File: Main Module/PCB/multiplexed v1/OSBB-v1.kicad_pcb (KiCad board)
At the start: 2 copper layers, 85.6 x 49.8 mm, 170 parts, among them P1 AUX 1-3, P14 EXTRA Pins, P2 Wire to Teensy VUSB, P3 +3.3V, P4 Pit, P5 Encoders, P6 BTN 1-32, Q1 NPN, Q2 NPN, Q3 NPN, Q4 NPN, U1 74HC4051, U2 74HC4051, U3 74HC4051, U4 74HC4051, U5 Teensy3.2

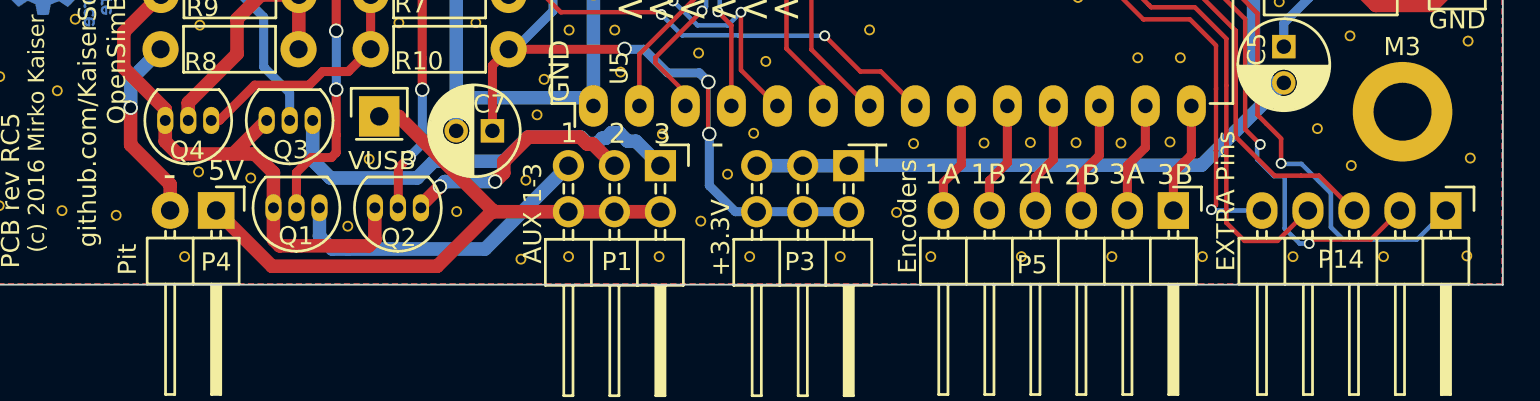
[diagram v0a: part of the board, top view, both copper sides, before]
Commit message: * added a few labels since I don't export all vlues for the gerber files * gerber files for RC5
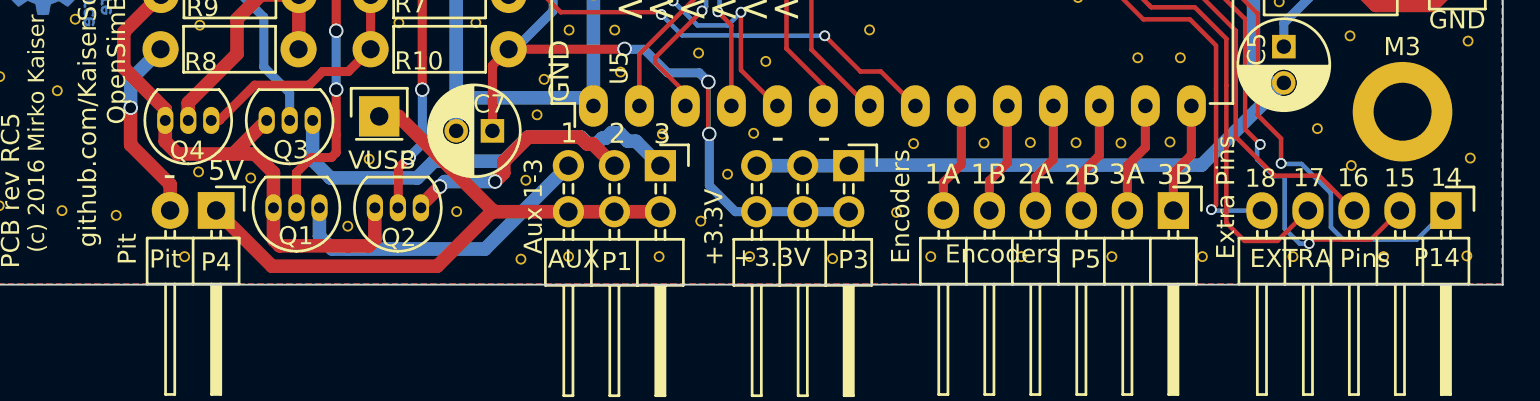
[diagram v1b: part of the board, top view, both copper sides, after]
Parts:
- P1: value AUX 1-3 -> AUX
- moved Ref** 0.43 mm to (223.9, 143.3)
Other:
- board text added: "+3.3V"
- board text added: "Aux 1-3"
- board text added: "Encoders"
- board text added: "Extra Pins"
- board text added: "Pit"
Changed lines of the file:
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@@
     (area 175.269999 88.074999 261.407144 151.803575)
     (thickness 1.6)
-    (drawings 96)
+    (drawings 106)
     (tracks 1158)
     (zones 0)
@@
       (drillshape 0)
       (scaleselection 1)
-      (outputdirectory ../Gerber-rev-RC4/))
+      (outputdirectory gerber/RC5/))
   )
   (net 0 "")
@@
   )
   (module MOBB-KiCad-Lib:VIA-W0.6mm-H0.4mm (layer F.Cu)
-    (at 224.33 143.22)
+    (at 223.91 143.33)
     (fp_text reference Ref** (at 0 0.5) (layer F.Fab) hide
       (effects (font (size 0.127 0.127) (thickness 0.000001)))
@@
       (effects (font (size 1 1) (thickness 0.15)))
     )
-    (fp_text value Pit (at 2.705 4.895 270) (layer F.SilkS)
+    (fp_text value Pit (at 2.69 2.82 360) (layer F.SilkS)
       (effects (font (size 1 1) (thickness 0.15)))
     )
@@
     (descr "Through hole pin header")
     (tags "pin header")
-    (fp_text reference P5 (at 3 7.8 360) (layer F.SilkS)
+    (fp_text reference P5 (at 2.685 4.845 360) (layer F.SilkS)
       (effects (font (size 1 1) (thickness 0.15)))
     )
-    (fp_text value Encoders (at 0.325 14.675 270) (layer F.SilkS)
+    (fp_text value Encoders (at 2.405 9.455 360) (layer F.SilkS)
       (effects (font (size 1 1) (thickness 0.15)))
     )
@@
       (effects (font (size 1 1) (thickness 0.15)))
     )
-    (fp_text value "AUX 1-3" (at 2.625 7.05 270) (layer F.SilkS)
+    (fp_text value AUX (at 5.16 4.78 360) (layer F.SilkS)
       (effects (font (size 1 1) (thickness 0.15)))
     )
@@
     (descr "Through hole pin header")
     (tags "pin header")
-    (fp_text reference P3 (at 5.3 2.7 360) (layer F.SilkS)
+    (fp_text reference P3 (at 5.19 -0.26 360) (layer F.SilkS)
       (effects (font (size 1 1) (thickness 0.15)))
     )
-    (fp_text value +3.3V (at 3.975 7.075 270) (layer F.SilkS)
+    (fp_text value +3.3V (at 5.07 4.23 360) (layer F.SilkS)
       (effects (font (size 1 1) (thickness 0.15)))
     )
@@
     (descr "Through hole pin header")
     (tags "pin header")
-    (fp_text reference P14 (at 2.7 5.8 360) (layer F.SilkS)
+    (fp_text reference P14 (at 2.605 0.505 360) (layer F.SilkS)
       (effects (font (size 1 1) (thickness 0.15)))
     )
-    (fp_text value "EXTRA Pins" (at -0.525 12.15 270) (layer F.SilkS)
+    (fp_text value "EXTRA Pins" (at 2.655 6.955 360) (layer F.SilkS)
       (effects (font (size 1 1) (thickness 0.15)))
     )
@@
       (net 6 GND) (zone_connect 2))
   )
+  (gr_text 14 (at 257.8 138.85) (layer F.SilkS)
+    (effects (font (size 1 1) (thickness 0.25)))
+  )
+  (gr_text 15 (at 255.22 138.88) (layer F.SilkS)
+    (effects (font (size 1 1) (thickness 0.25)))
+  )
+  (gr_text 16 (at 252.65 138.87) (layer F.SilkS)
+    (effects (font (size 1 1) (thickness 0.25)))
+  )
+  (gr_text 17 (at 250.21 138.87) (layer F.SilkS)
+    (effects (font (size 1 1) (thickness 0.25)))
+  )
+  (gr_text 18 (at 247.54 138.9) (layer F.SilkS)
+    (effects (font (size 1 1) (thickness 0.25)))
+  )
+  (gr_text "Extra Pins" (at 245.62 139.95 90) (layer F.SilkS)
+    (effects (font (size 1 1) (thickness 0.25)))
+  )
+  (gr_text Encoders (at 227.67 140.45 90) (layer F.SilkS)
+    (effects (font (size 1 1) (thickness 0.25)))
+  )
+  (gr_text +3.3V (at 217.36 141.6 90) (layer F.SilkS)
+    (effects (font (size 1 1) (thickness 0.25)))
+  )
+  (gr_text "Aux 1-3" (at 207.39 140.44 90) (layer F.SilkS)
+    (effects (font (size 1 1) (thickness 0.25)))
+  )
+  (gr_text Pit (at 184.97 142.8 90) (layer F.SilkS)
+    (effects (font (size 1 1) (thickness 0.25)))
+  )
   (gr_line (start 227.28 132.24) (end 227.28 129.5) (angle 90) (layer F.Fab) (width 0.2))
   (gr_line (start 239.14 132.24) (end 227.28 132.24) (angle 90) (layer F.Fab) (width 0.2))
@@
     (effects (font (size 1.2 1.2) (thickness 0.25)) (justify mirror))
   )
-  (gr_text - (at 226.65 136.925) (layer F.SilkS)
+  (gr_text - (at 223.44 136.61) (layer F.SilkS)
     (effects (font (size 1.5 1.5) (thickness 0.3)))
   )
-  (gr_text - (at 217.55 136.925) (layer F.SilkS)
+  (gr_text - (at 220.88 136.61) (layer F.SilkS)
     (effects (font (size 1.5 1.5) (thickness 0.3)))
   )
@@
     (effects (font (size 1 1) (thickness 0.25)))
   )
-  (gr_text VUSB (at 199.025 137.925) (layer F.SilkS)
+  (gr_text VUSB (at 199.03 137.9) (layer F.SilkS)
     (effects (font (size 1 1) (thickness 0.2)))
   )

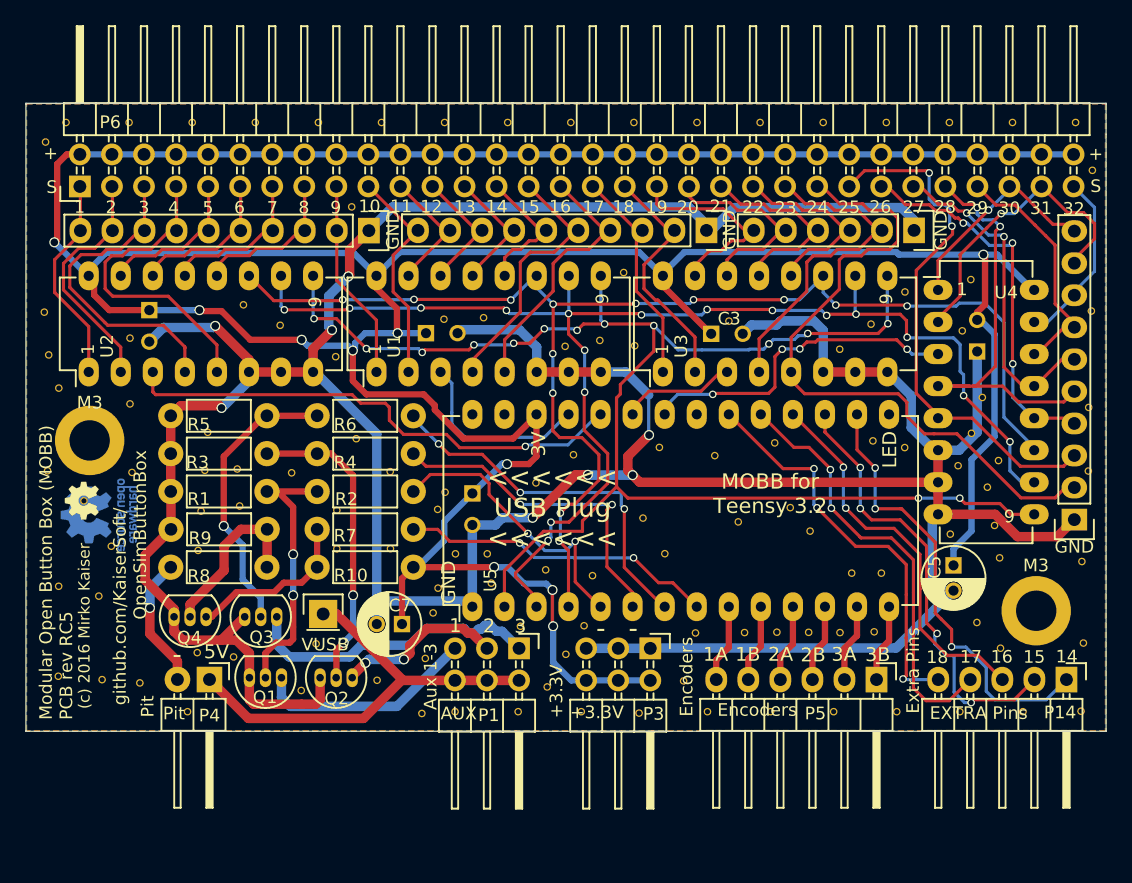
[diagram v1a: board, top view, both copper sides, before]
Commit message: * current work of PCB RC6 - WIP * added PTC fuses for 3.3V and 5V to protect the PC in case of accidental short circuit * added 2x1 straight pin header which connects to pin13. this may late be used for feedback. not used yet * added solder pads for optional SMD 0805 capacitors * position of mounting holes has moved again. now final and written on PCB back side * distance between pit, AUX, encoder, .... pin headers now multiples of 2.54mm
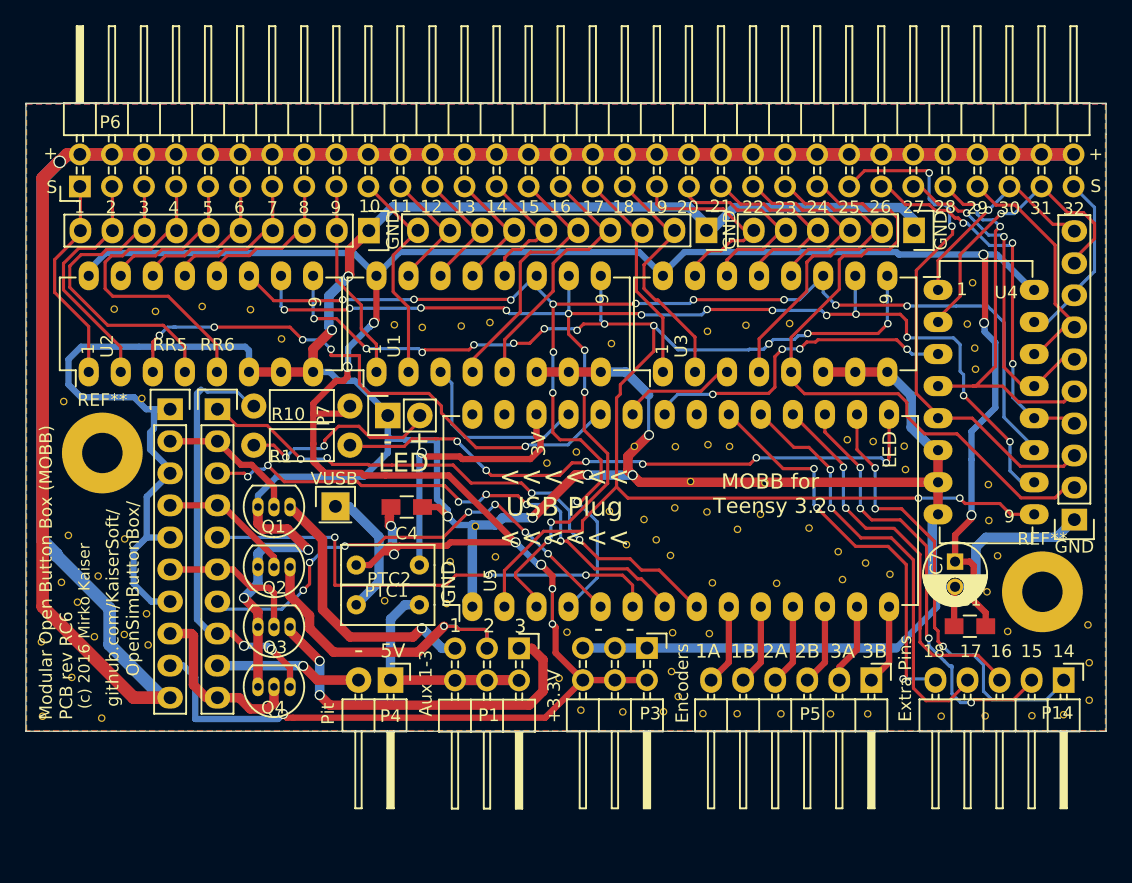
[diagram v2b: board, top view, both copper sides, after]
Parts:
- removed C2, C3, C6: C, Capacitors_ThroughHole:C_Disc_D3_P2.5
- removed C5: CP, Capacitors_ThroughHole:C_Radial_D5_L11_P2
- removed G***: LOGO, MOBB-KiCad-Lib:OPEN_HW_LOGO_3MM
- removed R2, R4, R6, R7, R8: 1K, Resistors_ThroughHole:Resistor_Horizontal_RM7mm
- removed R3, R5, R9: 10K, Resistors_ThroughHole:Resistor_Horizontal_RM7mm
- removed the REF** at (180.4, 121.7)
- removed the REF** at (255.4, 135.2)
- removed REF***: OSHW-Logo_5.7x6mm_Copper, Symbols:OSHW-Logo_5.7x6mm_Copper
- removed the Ref** at (252.4, 123.3)
- removed the Ref** at (229.3, 143.2)
- removed the Ref** at (177.9, 133.3)
- removed the Ref** at (177.9, 140.4)
- removed the Ref** at (184.3, 140.9)
- removed the Ref** at (188.1, 143.2)
- removed the Ref** at (188.9, 138.5)
- removed the Ref** at (191.8, 138.9)
- removed the Ref** at (198.3, 137.8)
- removed the Ref** at (197.1, 141.5)
- removed the Ref** at (206.7, 143.4)
- removed the Ref** at (209.3, 143.2)
- removed the Ref** at (223.9, 143.3)
- removed the Ref** at (214.5, 136.4)
- removed the Ref** at (219.6, 136.4)
- removed the Ref** at (218.1, 138.7)
- removed the Ref** at (216.6, 141.3)
- removed the Ref** at (228.4, 137.0)
- removed the Ref** at (227.4, 140.8)
- removed the Ref** at (252.6, 138.2)
- removed the Ref** at (250.7, 136.2)
- removed the Ref** at (259.1, 137.8)
- removed the Ref** at (259.0, 131.3)
- removed the Ref** at (219.3, 143.2)
- removed the Ref** at (252.5, 131.0)
- removed the Ref** at (252.1, 128.5)
- removed the Ref** at (248.6, 129.2)
- removed the Ref** at (235.9, 127.0)
- removed the Ref** at (237.5, 128.9)
- removed the Ref** at (231.8, 128.2)
- removed the Ref** at (225.9, 130.7)
- removed the Ref** at (243.1, 132.2)
- removed the Ref** at (240.8, 132.2)
- removed the Ref** at (224.2, 127.9)
- removed the Ref** at (214.3, 143.2)
- removed the Ref** at (178.5, 96.5)
- removed the Ref** at (183.5, 96.5)
- removed the Ref** at (188.5, 96.5)
- removed the Ref** at (193.5, 96.5)
- removed the Ref** at (198.5, 96.5)
- removed the Ref** at (203.5, 96.5)
- removed the Ref** at (250.2, 121.2)
- removed the Ref** at (208.5, 96.5)
- removed the Ref** at (213.5, 96.5)
- removed the Ref** at (218.5, 96.5)
- removed the Ref** at (223.5, 96.5)
- removed the Ref** at (228.5, 96.5)
- removed the Ref** at (233.5, 96.5)
- removed the Ref** at (238.5, 96.5)
- removed the Ref** at (243.5, 96.5)
- removed the Ref** at (248.5, 96.5)
- removed the Ref** at (253.5, 96.5)
- removed the Ref** at (251.1, 118.3)
- removed the Ref** at (245.0, 110.0)
- removed the Ref** at (222.7, 108.4)
- removed the Ref** at (200.0, 130.3)
- removed the Ref** at (200.0, 127.3)
- removed the Ref** at (196.4, 124.3)
- removed the Ref** at (192.1, 124.0)
- removed the Ref** at (192.3, 126.9)
- removed the Ref** at (207.0, 139.0)
- removed the Ref** at (203.2, 140.7)
- removed the Ref** at (242.5, 136.9)
- removed the Ref** at (258.9, 143.2)
- removed the Ref** at (239.8, 136.9)
- removed the Ref** at (237.3, 136.9)
- removed the Ref** at (234.8, 136.9)
- removed the Ref** at (232.3, 136.9)
- removed the Ref** at (245.0, 122.3)
- removed the Ref** at (242.4, 121.8)
- removed the Ref** at (201.1, 103.2)
- removed the Ref** at (234.7, 121.9)
- removed the Ref** at (249.2, 123.7)
- removed the Ref** at (251.5, 125.4)
- removed the Ref** at (254.3, 143.2)
- removed the Ref** at (259.5, 124.2)
- removed the Ref** at (259.5, 119.1)
- removed the Ref** at (259.8, 111.5)
- removed the Ref** at (250.2, 109.0)
- removed the Ref** at (249.5, 113.0)
- removed the Ref** at (242.3, 112.5)
- removed the Ref** at (239.8, 114.5)
- removed the Ref** at (231.0, 112.3)
- removed the Ref** at (223.6, 114.2)
- removed the Ref** at (220.8, 113.8)
- removed the Ref** at (249.3, 143.2)
- removed the Ref** at (218.1, 114.3)
- removed the Ref** at (208.4, 112.1)
- removed the Ref** at (211.6, 112.0)
- removed the Ref** at (199.9, 115.1)
- removed the Ref** at (195.5, 112.6)
- removed the Ref** at (192.6, 111.0)
- removed the Ref** at (183.6, 113.6)
- removed the Ref** at (183.7, 124.3)
- removed the Ref** at (183.6, 118.8)
- removed the Ref** at (177.9, 117.6)
- removed the Ref** at (244.3, 143.2)
- removed the Ref** at (189.7, 121.1)
- removed the Ref** at (189.5, 124.1)
- removed the Ref** at (189.2, 127.3)
- removed the Ref** at (189.0, 130.4)
- removed the Ref** at (204.2, 130.3)
- removed the Ref** at (204.2, 124.2)
- removed the Ref** at (201.5, 121.6)
- removed the Ref** at (220.2, 132.4)
- removed the Ref** at (216.5, 132.0)
- removed the Ref** at (209.4, 130.7)
- removed the Ref** at (239.3, 143.2)
- removed the Ref** at (211.9, 130.7)
- removed the Ref** at (212.2, 133.0)
- removed the Ref** at (207.6, 135.4)
- removed the Ref** at (208.0, 133.4)
- removed the Ref** at (207.9, 127.2)
- removed the Ref** at (208.5, 125.8)
- removed the Ref** at (215.7, 125.1)
- removed the Ref** at (218.7, 122.9)
- removed the Ref** at (229.9, 122.9)
- removed the Ref** at (225.5, 122.3)
- removed the Ref** at (234.3, 143.2)
- removed the Ref** at (259.8, 100.3)
- removed the Ref** at (258.5, 96.5)
- removed the Ref** at (176.9, 98.1)
- removed the Ref** at (176.8, 111.6)
- removed the Ref** at (177.1, 115.0)
- removed the Ref** at (177.0, 124.1)
- removed the Ref** at (179.9, 126.5)
- removed the Ref** at (182.1, 130.1)
- removed the Ref** at (181.4, 140.7)
- removed the Ref** at (181.1, 134.1)
- added P7: LED, Pin_Headers:Pin_Header_Straight_1x02, F.Cu at (204.0, 119.8)
- added PTC1: h0.3A/t0.5A, MOBB-KiCad-Lib:PTC-5MM, F.Cu at (204.0, 134.8)
- added PTC2: h0.3A/t0.5A, MOBB-KiCad-Lib:PTC-5MM, F.Cu at (204.0, 131.6)
- added REF**: MountingHole_3.2mm_M3_Pad, Mounting_Holes:MountingHole_3.2mm_M3_Pad, F.Cu at (181.4, 122.7)
- added REF**: MountingHole_3.2mm_M3_Pad, Mounting_Holes:MountingHole_3.2mm_M3_Pad, F.Cu at (255.9, 133.7)
- added RR5: 10K-STAR10, Pin_Headers:Pin_Header_Straight_1x10, F.Cu at (186.8, 119.2)
- added RR6: 1K-STAR10, Pin_Headers:Pin_Header_Straight_1x10, F.Cu at (190.5, 119.2)
- added Ref**: Val**, MOBB-KiCad-Lib:VIA-W0.6mm-H0.4mm, F.Cu at (251.5, 133.7)
- added Ref**: Val**, MOBB-KiCad-Lib:VIA-W0.6mm-H0.4mm, F.Cu at (229.4, 122.1)
- added Ref**: Val**, MOBB-KiCad-Lib:VIA-W0.6mm-H0.4mm, F.Cu at (223.5, 122.2)
- added Ref**: Val**, MOBB-KiCad-Lib:VIA-W0.6mm-H0.4mm, F.Cu at (225.3, 129.6)
- added Ref**: Val**, MOBB-KiCad-Lib:VIA-W0.6mm-H0.4mm, F.Cu at (229.3, 127.4)
- added Ref**: Val**, MOBB-KiCad-Lib:VIA-W0.6mm-H0.4mm, F.Cu at (233.5, 127.6)
- added Ref**: Val**, MOBB-KiCad-Lib:VIA-W0.6mm-H0.4mm, F.Cu at (195.6, 113.7)
- added Ref**: Val**, MOBB-KiCad-Lib:VIA-W0.6mm-H0.4mm, F.Cu at (183.2, 129.5)
- added Ref**: Val**, MOBB-KiCad-Lib:VIA-W0.6mm-H0.4mm, F.Cu at (208.9, 131.3)
- added Ref**: Val**, MOBB-KiCad-Lib:VIA-W0.6mm-H0.4mm, F.Cu at (216.6, 123.5)
- added Ref**: Val**, MOBB-KiCad-Lib:VIA-W0.6mm-H0.4mm, F.Cu at (218.9, 122.6)
- added Ref**: Val**, MOBB-KiCad-Lib:VIA-W0.6mm-H0.4mm, F.Cu at (253.1, 136.9)
- added Ref**: Val**, MOBB-KiCad-Lib:VIA-W0.6mm-H0.4mm, F.Cu at (210.9, 128.5)
- added Ref**: Val**, MOBB-KiCad-Lib:VIA-W0.6mm-H0.4mm, F.Cu at (203.8, 134.4)
- added Ref**: Val**, MOBB-KiCad-Lib:VIA-W0.6mm-H0.4mm, F.Cu at (208.7, 134.7)
- added Ref**: Val**, MOBB-KiCad-Lib:VIA-W0.6mm-H0.4mm, F.Cu at (226.5, 140.0)
- added Ref**: Val**, MOBB-KiCad-Lib:VIA-W0.6mm-H0.4mm, F.Cu at (227.0, 142.0)
- added Ref**: Val**, MOBB-KiCad-Lib:VIA-W0.6mm-H0.4mm, F.Cu at (224.3, 128.0)
- added Ref**: Val**, MOBB-KiCad-Lib:VIA-W0.6mm-H0.4mm, F.Cu at (226.7, 127.1)
- added Ref**: Val**, MOBB-KiCad-Lib:VIA-W0.6mm-H0.4mm, F.Cu at (217.6, 140.6)
- added Ref**: Val**, MOBB-KiCad-Lib:VIA-W0.6mm-H0.4mm, F.Cu at (218.2, 136.9)
- added Ref**: Val**, MOBB-KiCad-Lib:VIA-W0.6mm-H0.4mm, F.Cu at (229.7, 133.0)
- added Ref**: Val**, MOBB-KiCad-Lib:VIA-W0.6mm-H0.4mm, F.Cu at (184.5, 118.4)
- added Ref**: Val**, MOBB-KiCad-Lib:VIA-W0.6mm-H0.4mm, F.Cu at (234.8, 133.1)
- added Ref**: Val**, MOBB-KiCad-Lib:VIA-W0.6mm-H0.4mm, F.Cu at (240.0, 132.8)
- added Ref**: Val**, MOBB-KiCad-Lib:VIA-W0.6mm-H0.4mm, F.Cu at (226.6, 137.0)
- added Ref**: Val**, MOBB-KiCad-Lib:VIA-W0.6mm-H0.4mm, F.Cu at (229.5, 137.0)
- added Ref**: Val**, MOBB-KiCad-Lib:VIA-W0.6mm-H0.4mm, F.Cu at (219.3, 143.1)
- added Ref**: Val**, MOBB-KiCad-Lib:VIA-W0.6mm-H0.4mm, F.Cu at (222.6, 143.2)
- added Ref**: Val**, MOBB-KiCad-Lib:VIA-W0.6mm-H0.4mm, F.Cu at (225.8, 143.2)
- added Ref**: Val**, MOBB-KiCad-Lib:VIA-W0.6mm-H0.4mm, F.Cu at (229.0, 143.4)
- added Ref**: Val**, MOBB-KiCad-Lib:VIA-W0.6mm-H0.4mm, F.Cu at (231.7, 143.4)
- added Ref**: Val**, MOBB-KiCad-Lib:VIA-W0.6mm-H0.4mm, F.Cu at (235.2, 143.4)
- added Ref**: Val**, MOBB-KiCad-Lib:VIA-W0.6mm-H0.4mm, F.Cu at (184.9, 135.5)
- added Ref**: Val**, MOBB-KiCad-Lib:VIA-W0.6mm-H0.4mm, F.Cu at (239.1, 143.4)
- added Ref**: Val**, MOBB-KiCad-Lib:VIA-W0.6mm-H0.4mm, F.Cu at (242.0, 143.4)
- added Ref**: Val**, MOBB-KiCad-Lib:VIA-W0.6mm-H0.4mm, F.Cu at (247.8, 143.6)
- added Ref**: Val**, MOBB-KiCad-Lib:VIA-W0.6mm-H0.4mm, F.Cu at (251.3, 143.6)
- added Ref**: Val**, MOBB-KiCad-Lib:VIA-W0.6mm-H0.4mm, F.Cu at (255.0, 143.5)
- added Ref**: Val**, MOBB-KiCad-Lib:VIA-W0.6mm-H0.4mm, F.Cu at (257.6, 143.5)
- added Ref**: Val**, MOBB-KiCad-Lib:VIA-W0.6mm-H0.4mm, F.Cu at (259.6, 142.3)
- added Ref**: Val**, MOBB-KiCad-Lib:VIA-W0.6mm-H0.4mm, F.Cu at (259.5, 136.3)
- added Ref**: Val**, MOBB-KiCad-Lib:VIA-W0.6mm-H0.4mm, F.Cu at (259.6, 139.3)
- added Ref**: Val**, MOBB-KiCad-Lib:VIA-W0.6mm-H0.4mm, F.Cu at (245.0, 124.0)
- added Ref**: Val**, MOBB-KiCad-Lib:VIA-W0.6mm-H0.4mm, F.Cu at (185.0, 137.9)
- added Ref**: Val**, MOBB-KiCad-Lib:VIA-W0.6mm-H0.4mm, F.Cu at (244.9, 122.2)
- added Ref**: Val**, MOBB-KiCad-Lib:VIA-W0.6mm-H0.4mm, F.Cu at (242.5, 121.8)
- added Ref**: Val**, MOBB-KiCad-Lib:VIA-W0.6mm-H0.4mm, F.Cu at (240.4, 121.7)
- added Ref**: Val**, MOBB-KiCad-Lib:VIA-W0.6mm-H0.4mm, F.Cu at (231.1, 122.2)
- added Ref**: Val**, MOBB-KiCad-Lib:VIA-W0.6mm-H0.4mm, F.Cu at (226.8, 122.2)
- added Ref**: Val**, MOBB-KiCad-Lib:VIA-W0.6mm-H0.4mm, F.Cu at (233.9, 125.1)
- added Ref**: Val**, MOBB-KiCad-Lib:VIA-W0.6mm-H0.4mm, F.Cu at (228.0, 125.0)
- added Ref**: Val**, MOBB-KiCad-Lib:VIA-W0.6mm-H0.4mm, F.Cu at (212.5, 130.9)
- added Ref**: Val**, MOBB-KiCad-Lib:VIA-W0.6mm-H0.4mm, F.Cu at (221.6, 127.3)
- added Ref**: Val**, MOBB-KiCad-Lib:VIA-W0.6mm-H0.4mm, F.Cu at (222.9, 130.0)
- added Ref**: Val**, MOBB-KiCad-Lib:VIA-W0.6mm-H0.4mm, F.Cu at (183.1, 137.1)
- added Ref**: Val**, MOBB-KiCad-Lib:VIA-W0.6mm-H0.4mm, F.Cu at (226.4, 130.8)
- added Ref**: Val**, MOBB-KiCad-Lib:VIA-W0.6mm-H0.4mm, F.Cu at (231.7, 128.8)
- added Ref**: Val**, MOBB-KiCad-Lib:VIA-W0.6mm-H0.4mm, F.Cu at (237.4, 128.7)
- added Ref**: Val**, MOBB-KiCad-Lib:VIA-W0.6mm-H0.4mm, F.Cu at (239.7, 130.5)
- added Ref**: Val**, MOBB-KiCad-Lib:VIA-W0.6mm-H0.4mm, F.Cu at (241.9, 131.4)
- added Ref**: Val**, MOBB-KiCad-Lib:VIA-W0.6mm-H0.4mm, F.Cu at (243.8, 132.3)
- added Ref**: Val**, MOBB-KiCad-Lib:VIA-W0.6mm-H0.4mm, F.Cu at (252.3, 130.9)
- added Ref**: Val**, MOBB-KiCad-Lib:VIA-W0.6mm-H0.4mm, F.Cu at (251.6, 128.1)
- added Ref**: Val**, MOBB-KiCad-Lib:VIA-W0.6mm-H0.4mm, F.Cu at (251.6, 125.2)
- added Ref**: Val**, MOBB-KiCad-Lib:VIA-W0.6mm-H0.4mm, F.Cu at (250.3, 109.2)
- added Ref**: Val**, MOBB-KiCad-Lib:VIA-W0.6mm-H0.4mm, F.Cu at (181.1, 132.5)
- added Ref**: Val**, MOBB-KiCad-Lib:VIA-W0.6mm-H0.4mm, F.Cu at (250.6, 116.1)
- added Ref**: Val**, MOBB-KiCad-Lib:VIA-W0.6mm-H0.4mm, F.Cu at (250.5, 114.4)
- added Ref**: Val**, MOBB-KiCad-Lib:VIA-W0.6mm-H0.4mm, F.Cu at (249.9, 112.5)
- added Ref**: Val**, MOBB-KiCad-Lib:VIA-W0.6mm-H0.4mm, F.Cu at (235.8, 112.5)
- added Ref**: Val**, MOBB-KiCad-Lib:VIA-W0.6mm-H0.4mm, F.Cu at (232.4, 112.6)
- added Ref**: Val**, MOBB-KiCad-Lib:VIA-W0.6mm-H0.4mm, F.Cu at (229.3, 113.1)
- added Ref**: Val**, MOBB-KiCad-Lib:VIA-W0.6mm-H0.4mm, F.Cu at (221.7, 114.0)
- added Ref**: Val**, MOBB-KiCad-Lib:VIA-W0.6mm-H0.4mm, F.Cu at (212.1, 112.4)
- added Ref**: Val**, MOBB-KiCad-Lib:VIA-W0.6mm-H0.4mm, F.Cu at (209.8, 112.7)
- added Ref**: Val**, MOBB-KiCad-Lib:VIA-W0.6mm-H0.4mm, F.Cu at (206.7, 112.8)
- added Ref**: Val**, MOBB-KiCad-Lib:VIA-W0.6mm-H0.4mm, F.Cu at (179.4, 134.5)
- added Ref**: Val**, MOBB-KiCad-Lib:VIA-W0.6mm-H0.4mm, F.Cu at (204.5, 112.6)
- added Ref**: Val**, MOBB-KiCad-Lib:VIA-W0.6mm-H0.4mm, F.Cu at (193.1, 111.4)
- added Ref**: Val**, MOBB-KiCad-Lib:VIA-W0.6mm-H0.4mm, F.Cu at (189.3, 111.1)
- added Ref**: Val**, MOBB-KiCad-Lib:VIA-W0.6mm-H0.4mm, F.Cu at (185.6, 111.5)
- added Ref**: Val**, MOBB-KiCad-Lib:VIA-W0.6mm-H0.4mm, F.Cu at (182.3, 111.3)
- added Ref**: Val**, MOBB-KiCad-Lib:VIA-W0.6mm-H0.4mm, F.Cu at (178.3, 118.6)
- added Ref**: Val**, MOBB-KiCad-Lib:VIA-W0.6mm-H0.4mm, F.Cu at (178.7, 129.2)
- added Ref**: Val**, MOBB-KiCad-Lib:VIA-W0.6mm-H0.4mm, F.Cu at (181.3, 143.7)
- added Ref**: Val**, MOBB-KiCad-Lib:VIA-W0.6mm-H0.4mm, F.Cu at (179.0, 140.5)
- added Ref**: Val**, MOBB-KiCad-Lib:VIA-W0.6mm-H0.4mm, F.Cu at (176.6, 137.7)
- added Ref**: Val**, MOBB-KiCad-Lib:VIA-W0.6mm-H0.4mm, F.Cu at (176.6, 143.6)
- added Ref**: Val**, MOBB-KiCad-Lib:VIA-W0.6mm-H0.4mm, F.Cu at (180.8, 137.3)
- added Ref**: Val**, MOBB-KiCad-Lib:VIA-W0.6mm-H0.4mm, F.Cu at (178.1, 133.0)
- C1, C4: footprint Capacitors_ThroughHole:C_Disc_D3_P2.5 -> Capacitors_SMD:C_0805_HandSoldering; moved to F.Cu
- P1: value AUX -> AUX 1-3
- P4: value Pit -> Pit Limiter
- P5: value Encoders -> Rotary Encoders
- moved C1 69.7 mm to (250.1, 136.4), turned to 0 degrees
- moved C4 46.9 mm to (205.5, 127.0), turned to 180 degrees
- moved C7 44.1 mm to (248.9, 131.3), turned to 270 degrees
- moved P4 14.3 mm to (204.2, 140.7)
- moved R10 13.7 mm to (201.0, 119.0)
- moved Q1 13.5 mm to (196.2, 127.0)
- moved Q2 10.1 mm to (196.2, 131.8)
- moved Q4 8.66 mm to (196.2, 141.2)
- moved P2 8.58 mm to (199.8, 127.0)
- moved R1 7.53 mm to (201.0, 122.1)
- moved Q3 1.32 mm to (196.2, 136.5)
- moved P5 0.41 mm to (242.3, 140.7)
- moved P3 0.27 mm to (224.5, 138.2)
- moved P14 0.22 mm to (257.6, 140.7)
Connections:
- C1 pad 1: +3V3 -> GND
- C1 pad 2: GND -> +3V3
- P2 pad 1: +5V -> Net-(P2-Pad1)
- P6 pad 10: +3V3 -> PINHEADERSRC
- P6 pad 12: +3V3 -> PINHEADERSRC
- P6 pad 14: +3V3 -> PINHEADERSRC
- P6 pad 16: +3V3 -> PINHEADERSRC
- P6 pad 18: +3V3 -> PINHEADERSRC
- P6 pad 2: +3V3 -> PINHEADERSRC
- P6 pad 20: +3V3 -> PINHEADERSRC
- P6 pad 22: +3V3 -> PINHEADERSRC
- P6 pad 24: +3V3 -> PINHEADERSRC
- P6 pad 26: +3V3 -> PINHEADERSRC
- P6 pad 28: +3V3 -> PINHEADERSRC
- P6 pad 30: +3V3 -> PINHEADERSRC
- P6 pad 32: +3V3 -> PINHEADERSRC
- P6 pad 34: +3V3 -> PINHEADERSRC
- P6 pad 36: +3V3 -> PINHEADERSRC
- P6 pad 38: +3V3 -> PINHEADERSRC
- P6 pad 4: +3V3 -> PINHEADERSRC
- P6 pad 40: +3V3 -> PINHEADERSRC
- P6 pad 42: +3V3 -> PINHEADERSRC
- P6 pad 44: +3V3 -> PINHEADERSRC
- P6 pad 46: +3V3 -> PINHEADERSRC
- P6 pad 48: +3V3 -> PINHEADERSRC
- P6 pad 50: +3V3 -> PINHEADERSRC
- P6 pad 52: +3V3 -> PINHEADERSRC
- P6 pad 54: +3V3 -> PINHEADERSRC
- P6 pad 56: +3V3 -> PINHEADERSRC
- P6 pad 58: +3V3 -> PINHEADERSRC
- P6 pad 6: +3V3 -> PINHEADERSRC
- P6 pad 60: +3V3 -> PINHEADERSRC
- P6 pad 62: +3V3 -> PINHEADERSRC
- P6 pad 64: +3V3 -> PINHEADERSRC
- P6 pad 8: +3V3 -> PINHEADERSRC
- R1 pad 1: Net-(Q1-Pad2) -> Net-(R1-Pad1)
- R1 pad 2: GND -> Net-(P7-Pad2)
- U5 pad 15: Net-(U5-Pad15) -> Net-(R1-Pad1)
- U5 pad 21: /reserved_for_4051 -> (no net)
- U5 pad 26: +3V3 -> Net-(PTC2-Pad2)
- U5 pad 27: Net-(U5-Pad27) -> (no net)
- U5 pad 28: Net-(U5-Pad28) -> (no net)
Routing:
- net PINHEADERSRC: track 0.00 -> 334.6 mm, vias 0 -> 1
- net +3V3: track 311.8 -> 236.6 mm, vias 10 -> 12
- net Net-(R1-Pad1): track 0.00 -> 49.1 mm, vias 0 -> 6
- net Net-(PTC2-Pad2): track 0.00 -> 22.4 mm, vias 0 -> 1
- net Net-(RR6-Pad1): track 25.3 -> 45.8 mm, vias 2 -> 4
- net Net-(Q4-Pad1): track 13.4 -> 33.3 mm, vias 0 -> 2
- net Net-(P7-Pad2): track 0.00 -> 16.2 mm, vias 0 -> 2
- net Net-(RR6-Pad7): track 22.7 -> 38.5 mm, vias 2 -> 7
- net Net-(P1-Pad3): track 13.6 -> 27.6 mm, vias 2 -> 1
- net Net-(Q2-Pad2): track 24.1 -> 10.3 mm, vias 2 -> 0
- net Net-(RR6-Pad3): track 29.7 -> 43.3 mm, vias 3 -> 6
- net +5V: track 35.9 -> 22.9 mm
- net Net-(RR6-Pad5): track 26.6 -> 39.1 mm, vias 2 -> 3
- net Net-(Q3-Pad2): track 22.9 -> 11.9 mm, vias 1 -> 0
- net Net-(P2-Pad1): track 0.00 -> 10.6 mm
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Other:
- net class 3.3PIN added: clearance 0.3, trace_width 1, via_dia 1, via_drill 0.8
- board text added: "11mm"
- board text added: "22mm"
- board text added: "5mm"
- board text added: "6mm"
- board text added: "Modular Open Button Box (MOBB) PCB rev RC6"
- board text added: "github.com/KaiserSoft/ OpenSimButtonBox/"
- board text removed: "Modular Open Button Box (MOBB) PCB rev RC5"
- board text removed: "github.com/KaiserSoft/ OpenSimButtonBox"
